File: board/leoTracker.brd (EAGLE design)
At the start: 72.8 x 31.6 mm, 54 parts, among them J1 AVR_SPI_PRG_6PTH, Q1 MOSFET-NCHANNELSMD, U3 ATMEGA32U4, X1 USB-MINIB-5PIN, Y1 16MHz

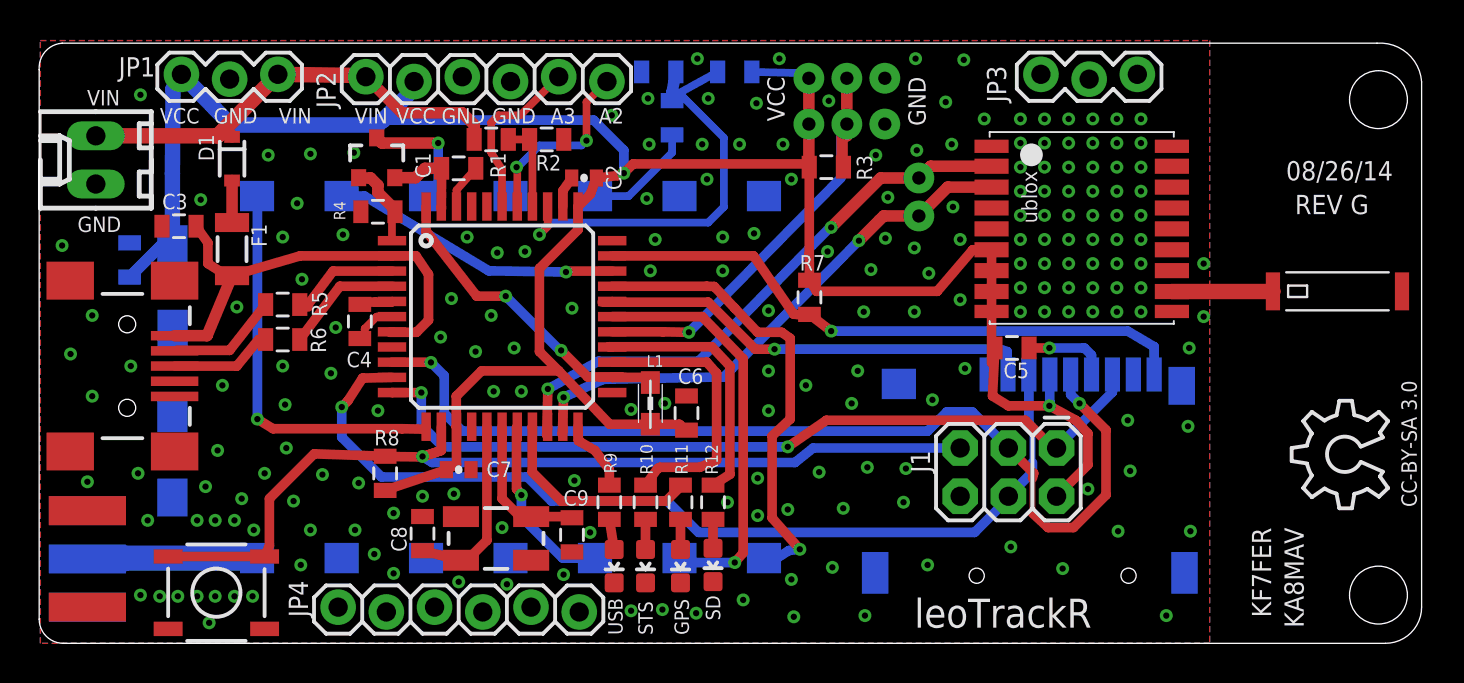
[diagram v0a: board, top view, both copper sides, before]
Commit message: Latest version: Used new SA818 footprint; changed crystal; cleaned up silkscreen for fabrication
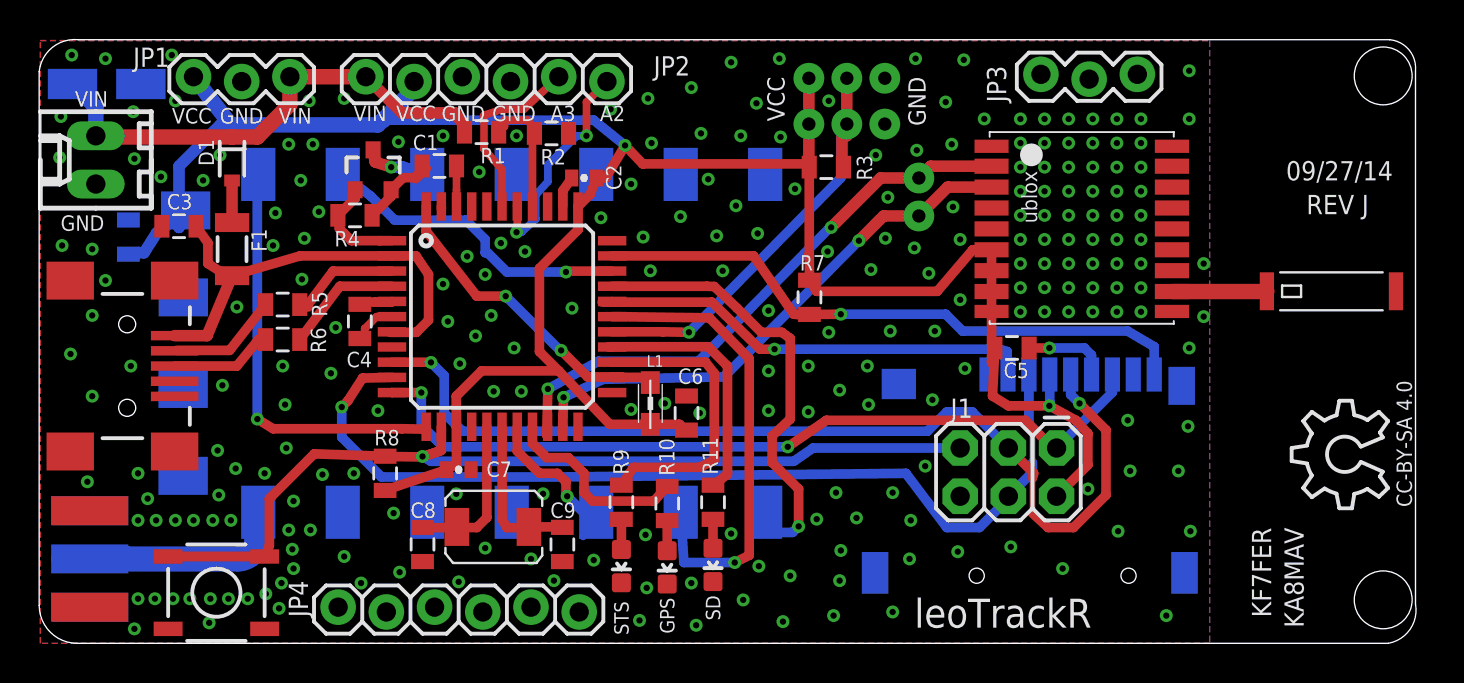
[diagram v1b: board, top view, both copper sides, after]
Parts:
- removed C10: 1uF, SparkFun:0805
- removed D2: Amber, SparkFun-LED:LED-0603
- removed R12: 330, SparkFun-Passives:0805
- removed R13, R14: 1K, SparkFun-Passives:0805
- added C12: (no value), rcl:153CLV-0405
- U$7: device BLOATEDnicerf:SA818 -> nicerf:SA818
- Y1: device SparkFun:CRYSTAL-SMD-5X3 -> newAva:ABRACON_ABM3_CRYSTAL
- moved U$7 1.78 mm to (24.8, 15.2)
- moved R11 1.71 mm to (35.4, 7.43)
- moved Y1 1.43 mm to (25.3, 6.03)
- moved STANDOFF1 1.27 mm to (70.7, 29.9)
- moved D3 1.27 mm to (30.6, 4.06)
- moved R4 1.22 mm to (16.6, 22.5), turned to 180 degrees
- moved C14 1.21 mm to (4.64, 21.4)
- moved R10 1.14 mm to (33.0, 7.37)
- moved C1 1.02 mm to (21.0, 25.1)
- moved C9 0.72 mm to (27.5, 5.21)
- moved D4 0.70 mm to (33.0, 4.00)
- moved Q1 0.66 mm to (17.5, 24.9)
- moved JP1 0.65 mm to (8.06, 29.7)
- moved R1 0.63 mm to (23.2, 26.9)
- moved R9 0.63 mm to (30.6, 7.43)
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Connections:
- removed net N$16: D2.A, R9.2
- removed net N$9: C10.2, U$7.P$3
- net A0: no longer C10.1, R13.2, R14.1
- net D12: now also R11.1; no longer R12.1
- net D2: now also R10.1; no longer R11.1
- net D4: now also R9.1; no longer R10.1
- net GND: now also C12.-; no longer D2.C, R13.1
- net N$1: now also Y1.P$1; no longer Y1.1
- net N$10: now also R11.2; no longer R12.2
- net N$2: now also Y1.P$2; no longer Y1.3
- net N$5: now also R9.2; no longer R10.2
- net N$7: now also R10.2; no longer R11.2
- net USB_TX: no longer R9.1
- net VCC: no longer R14.2
- net VIN: now also C12.+
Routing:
- net A0: track 23.2 -> 0.00 mm, vias 1 -> 0
- net N$9: track 5.95 -> 0.00 mm
- net USB_TX: track 3.83 -> 0.00 mm
- net VCC: track 131.8 -> 128.0 mm
- net PTT: track 6.48 -> 3.49 mm
- net D8: track 21.7 -> 24.7 mm
- net VIN: track 23.7 -> 26.4 mm
- net A1: track 4.72 -> 6.77 mm
- net N$20: track 14.0 -> 16.0 mm
- net A2: track 9.91 -> 11.8 mm
- net N$16: track 1.61 -> 0.00 mm
- net N$1: track 10.0 -> 8.56 mm
- net D5: track 15.4 -> 16.7 mm
- net N$2: track 7.89 -> 9.07 mm
- net D11: track 20.8 -> 22.0 mm
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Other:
- board size 72.8 x 31.6 mm -> 72.5 x 31.8 mm
- board text added: "09/27/14"
- board text added: "CC-BY-SA 4.0"
- board text added: "REV J"
- board text removed: "08/26/14"
- board text removed: "CC-BY-SA 3.0"
- board text removed: "REV G"
- board text removed: "USB"
